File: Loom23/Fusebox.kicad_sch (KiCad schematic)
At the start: 0 parts

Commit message: Added detailed version of schematic
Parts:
- added F? (x8): (no value), symbol Device:Fuse
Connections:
- new net ECU+12V: F?.2
- new net From LVMS: F?.1, F?.1, F?.2
- new net Fuel pump power: F?.2
- new net Fused +12V: F?.1
- new net INJ 1,3 +12V: F?.2
- new net INJ 2,4 +12V: F?.2
- new net Lambda sensor power: F?.2
- new net Relays fuelpump: F?.1, F?.1
- new net Relays injectors: F?.1, F?.1
- new net Relays power +12V: F?.2
- new net Relays spark: F?.1
- new net Spark+: F?.2

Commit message: Signed-off-by: fst29 <fst29@cam.ac.uk>
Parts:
- F?: value (none) -> 5A (Lambda sensor)
- F?: value (none) -> 5A (INJ 2,4)
- F?: value (none) -> 2A (ECU)
- F?: value (none) -> 5A (INJ 1,3)
- F?: value (none) -> TBD A (Spark)
- F?: value (none) -> 30A (Our circuits)
- F?: value (none) -> 10A (Fuel pump)
- F?: value (none) -> 20A (FP+INJ)
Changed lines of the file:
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@@
       (effects (font (size 1.27 1.27)) (justify left))
     )
-    (property "Value" "" (id 1) (at 189.23 78.7399 0)
+    (property "Value" "5A (Lambda sensor)" (id 1) (at 189.23 78.7399 0)
       (effects (font (size 1.27 1.27)) (justify left))
     )
@@
       (effects (font (size 1.27 1.27)) (justify left))
     )
-    (property "Value" "" (id 1) (at 151.13 78.7399 0)
+    (property "Value" "5A (INJ 2,4)" (id 1) (at 151.13 78.7399 0)
       (effects (font (size 1.27 1.27)) (justify left))
     )
@@
       (effects (font (size 1.27 1.27)) (justify left))
     )
-    (property "Value" "" (id 1) (at 82.55 78.7399 0)
+    (property "Value" "2A (ECU)" (id 1) (at 82.55 78.7399 0)
       (effects (font (size 1.27 1.27)) (justify left))
     )
@@
       (effects (font (size 1.27 1.27)) (justify left))
     )
-    (property "Value" "" (id 1) (at 134.62 78.7399 0)
+    (property "Value" "5A (INJ 1,3)" (id 1) (at 134.62 78.7399 0)
       (effects (font (size 1.27 1.27)) (justify left))
     )
@@
       (effects (font (size 1.27 1.27)) (justify left))
     )
-    (property "Value" "" (id 1) (at 215.9 78.7399 0)
+    (property "Value" "TBD A (Spark)" (id 1) (at 215.9 78.7399 0)
       (effects (font (size 1.27 1.27)) (justify left))
     )
@@
       (effects (font (size 1.27 1.27)) (justify right))
     )
-    (property "Value" "" (id 1) (at 113.03 78.7399 0)
+    (property "Value" "30A (Our circuits)" (id 1) (at 113.03 78.7399 0)
       (effects (font (size 1.27 1.27)) (justify right))
     )
@@
       (effects (font (size 1.27 1.27)) (justify left))
     )
-    (property "Value" "" (id 1) (at 167.64 78.7399 0)
+    (property "Value" "10A (Fuel pump)" (id 1) (at 167.64 78.7399 0)
       (effects (font (size 1.27 1.27)) (justify left))
     )
@@
       (effects (font (size 1.27 1.27)) (justify left))
     )
-    (property "Value" "" (id 1) (at 95.25 78.7399 0)
+    (property "Value" "20A (FP+INJ)" (id 1) (at 95.25 78.7399 0)
       (effects (font (size 1.27 1.27)) (justify left))
     )

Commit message: Added current ratings
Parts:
- F?: value 20A (FP+INJ) -> 50A
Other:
- note added: "(FP+INJ+SPK+LAMBDA+FANS)"
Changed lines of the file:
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@@
     (stroke (width 0) (type default) (color 0 0 0 0))
+  )
+  (text "(FP+INJ+SPK+LAMBDA+FANS)" (at 95.25 81.28 0)
+    (effects (font (size 0.5 0.5)) (justify left bottom))
   )
   (hierarchical_label "Relays injectors" (shape input) (at 132.08 67.31 90)
@@
       (effects (font (size 1.27 1.27)) (justify left))
     )
-    (property "Value" "20A (FP+INJ)" (id 1) (at 95.25 78.7399 0)
+    (property "Value" "50A" (id 1) (at 95.25 78.7399 0)
       (effects (font (size 1.27 1.27)) (justify left))
     )

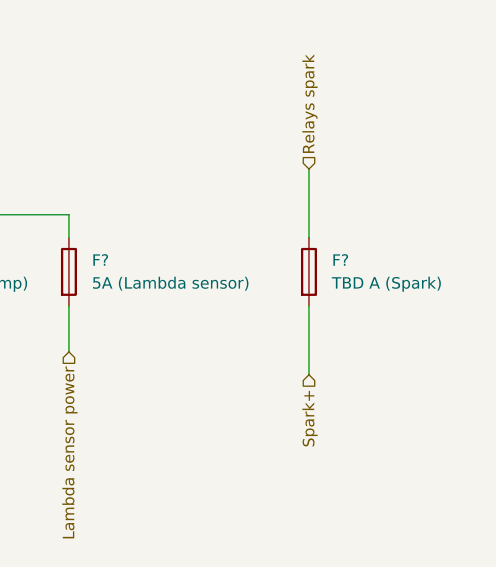
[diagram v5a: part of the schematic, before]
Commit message: Added temp reqs and fuse values
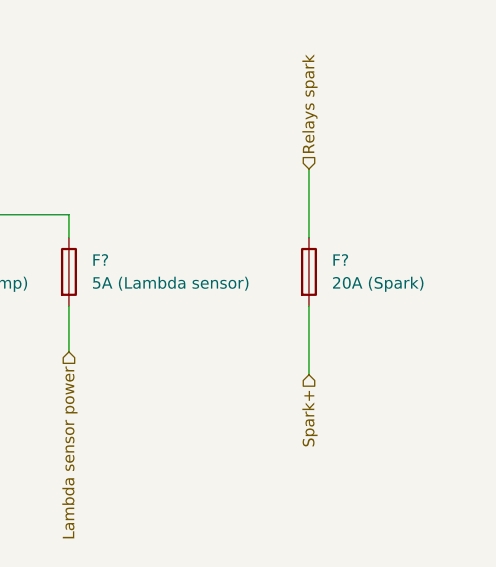
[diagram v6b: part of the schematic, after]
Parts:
- F?: value TBD A (Spark) -> 20A (Spark)
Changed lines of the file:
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@@
       (effects (font (size 1.27 1.27)) (justify left))
     )
-    (property "Value" "TBD A (Spark)" (id 1) (at 215.9 78.7399 0)
+    (property "Value" "20A (Spark)" (id 1) (at 215.9 78.7399 0)
       (effects (font (size 1.27 1.27)) (justify left))
     )

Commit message: Changes made to fusebox, relayboard and camsensor
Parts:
- removed F?: 50A, symbol Device:Fuse
- added F?: 20A (Fans), symbol Device:Fuse
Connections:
- new net Fans: F?.2
- new net Relays fans: F?.1
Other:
- note removed: "(FP+INJ+SPK+LAMBDA+FANS)"
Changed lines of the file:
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@@
 (kicad_sch (version 20211123) (generator eeschema)
   (paper "A4")
-  (junction (at 92.71 68.58) (diameter 0) (color 0 0 0 0)
-  )
   (junction (at 132.08 71.12) (diameter 0) (color 0 0 0 0)
   )
@@
     (stroke (width 0) (type default) (color 0 0 0 0))
   )
+  (wire (pts (xy 233.68 81.28) (xy 233.68 88.9))
+    (stroke (width 0) (type default) (color 0 0 0 0))
+  )
   (wire (pts (xy 213.36 66.04) (xy 213.36 73.66))
     (stroke (width 0) (type default) (color 0 0 0 0))
@@
     (stroke (width 0) (type default) (color 0 0 0 0))
   )
-  (wire (pts (xy 92.71 68.58) (xy 92.71 73.66))
-    (stroke (width 0) (type default) (color 0 0 0 0))
-  )
-  (wire (pts (xy 110.49 68.58) (xy 92.71 68.58))
-    (stroke (width 0) (type default) (color 0 0 0 0))
-  )
   (wire (pts (xy 186.69 81.28) (xy 186.69 86.36))
     (stroke (width 0) (type default) (color 0 0 0 0))
@@
     (stroke (width 0) (type default) (color 0 0 0 0))
   )
-  (wire (pts (xy 92.71 68.58) (xy 80.01 68.58))
+  (wire (pts (xy 80.01 68.58) (xy 110.49 68.58))
     (stroke (width 0) (type default) (color 0 0 0 0))
   )
@@
     (stroke (width 0) (type default) (color 0 0 0 0))
   )
-  (wire (pts (xy 92.71 81.28) (xy 92.71 86.36))
-    (stroke (width 0) (type default) (color 0 0 0 0))
-  )
   (wire (pts (xy 165.1 71.12) (xy 165.1 73.66))
     (stroke (width 0) (type default) (color 0 0 0 0))
   )
+  (wire (pts (xy 233.68 66.04) (xy 233.68 73.66))
+    (stroke (width 0) (type default) (color 0 0 0 0))
+  )
   (wire (pts (xy 148.59 81.28) (xy 148.59 86.36))
     (stroke (width 0) (type default) (color 0 0 0 0))
@@
     (stroke (width 0) (type default) (color 0 0 0 0))
   )
-  (text "(FP+INJ+SPK+LAMBDA+FANS)" (at 95.25 81.28 0)
-    (effects (font (size 0.5 0.5)) (justify left bottom))
-  )
   (hierarchical_label "Relays injectors" (shape input) (at 132.08 67.31 90)
     (effects (font (size 1.27 1.27)) (justify left))
   )
+  (hierarchical_label "Relays fans" (shape input) (at 233.68 66.04 90)
+    (effects (font (size 1.27 1.27)) (justify left))
+  )
   (hierarchical_label "INJ 2,4 +12V" (shape input) (at 148.59 86.36 270)
     (effects (font (size 1.27 1.27)) (justify right))
   )
+  (hierarchical_label "Fans" (shape input) (at 233.68 88.9 270)
+    (effects (font (size 1.27 1.27)) (justify right))
+  )
   (hierarchical_label "Fuel pump power" (shape input) (at 165.1 86.36 270)
     (effects (font (size 1.27 1.27)) (justify right))
@@
     (effects (font (size 1.27 1.27)) (justify right))
   )
-  (hierarchical_label "Relays power +12V" (shape input) (at 92.71 86.36 270)
-    (effects (font (size 1.27 1.27)) (justify right))
-  )
   (hierarchical_label "Fused +12V" (shape input) (at 110.49 86.36 270)
     (effects (font (size 1.27 1.27)) (justify right))
@@
     )
     (property "Datasheet" "~" (id 3) (at 186.69 77.47 0)
+      (effects (font (size 1.27 1.27)) hide)
+    )
+    (pin "1")
+    (pin "2")
+  )
+  (symbol (lib_id "Device:Fuse") (at 233.68 77.47 0) (unit 1)
+    (in_bom yes) (on_board yes) (fields_autoplaced)
+    (property "Reference" "F?" (id 0) (at 236.22 76.1999 0)
+      (effects (font (size 1.27 1.27)) (justify left))
+    )
+    (property "Value" "20A (Fans)" (id 1) (at 236.22 78.7399 0)
+      (effects (font (size 1.27 1.27)) (justify left))
+    )
+    (property "Footprint" "" (id 2) (at 231.902 77.47 90)
+      (effects (font (size 1.27 1.27)) hide)
+    )
+    (property "Datasheet" "~" (id 3) (at 233.68 77.47 0)
       (effects (font (size 1.27 1.27)) hide)
     )
@@
       (effects (font (size 1.27 1.27)) hide)
     )
-    (pin "1")
-    (pin "2")
-  )
-  (symbol (lib_id "Device:Fuse") (at 92.71 77.47 0) (unit 1)
-    (in_bom yes) (on_board yes) (fields_autoplaced)
-    (property "Reference" "F?" (id 0) (at 95.25 76.1999 0)
-      (effects (font (size 1.27 1.27)) (justify left))
-    )
-    (property "Value" "50A" (id 1) (at 95.25 78.7399 0)
-      (effects (font (size 1.27 1.27)) (justify left))
-    )
-    (property "Footprint" "" (id 2) (at 90.932 77.47 90)
-      (effects (font (size 1.27 1.27)) hide)
-    )
-    (property "Datasheet" "~" (id 3) (at 92.71 77.47 0)
-      (effects (font (size 1.27 1.27)) hide)
-    )

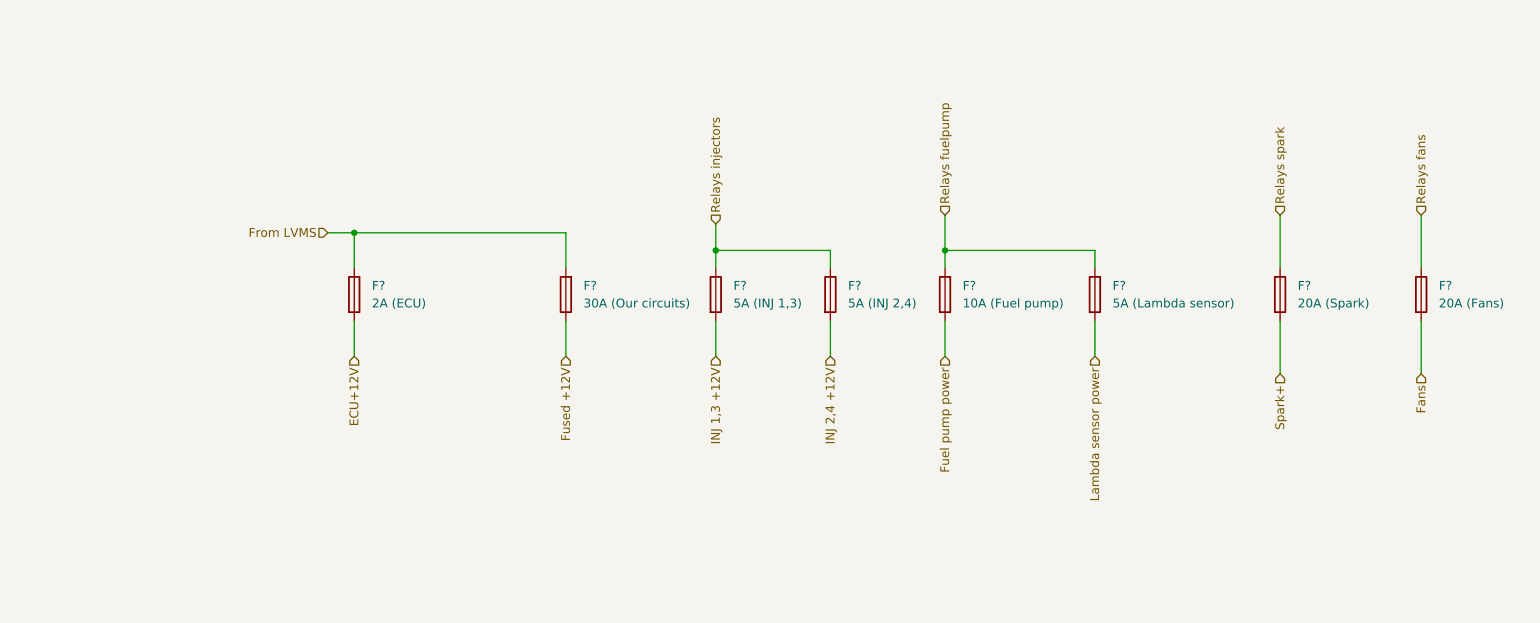
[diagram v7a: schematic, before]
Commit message: Changed labels to match old wires
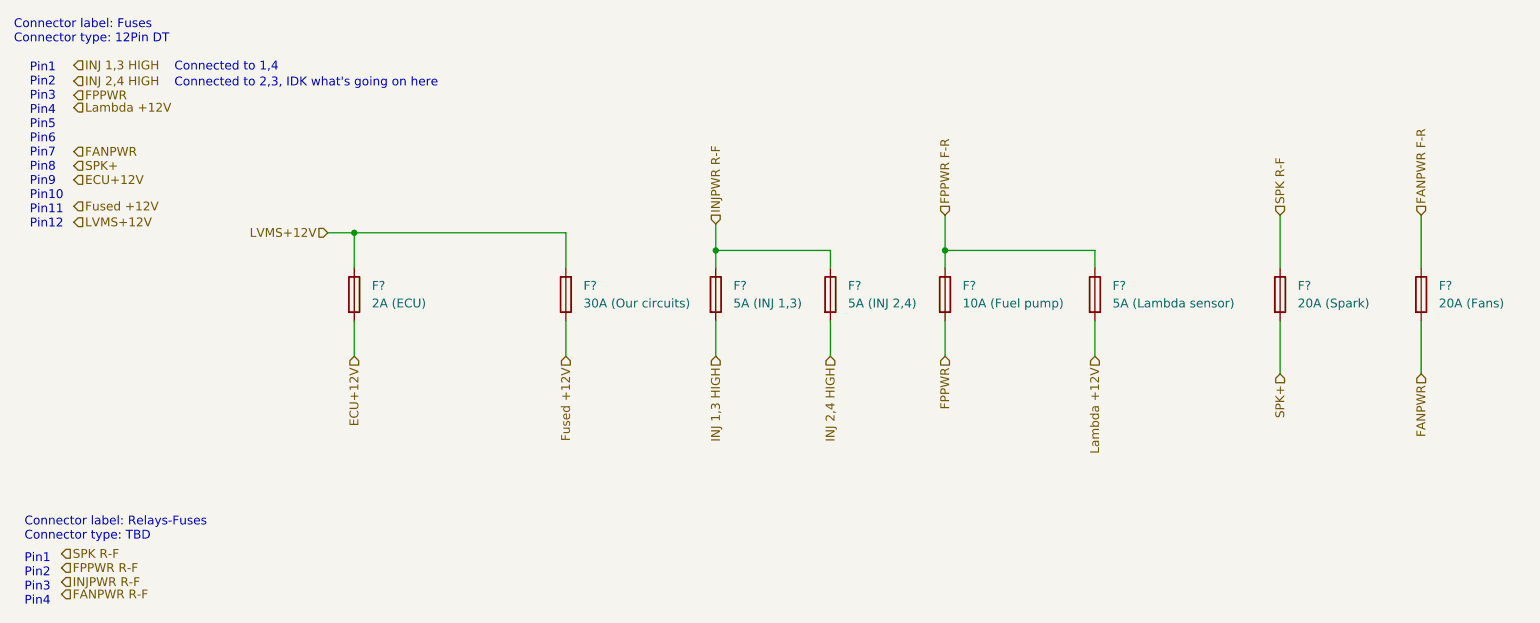
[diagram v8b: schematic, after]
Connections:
- net Fans renamed FANPWR
- net From LVMS renamed LVMS+12V
- net Fuel pump power renamed FPPWR
- net INJ 1,3 +12V renamed INJ 1,3 HIGH
- net INJ 2,4 +12V renamed INJ 2,4 HIGH
- net Lambda sensor power renamed Lambda +12V
- net Relays fans renamed FANPWR F-R
- net Relays fuelpump renamed FPPWR F-R
- net Relays injectors renamed INJPWR R-F
- net Relays spark renamed SPK R-F
- net Spark+ renamed SPK+
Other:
- note added: "Connected to 1,4"
- note added: "Connected to 2,3, IDK what's going on here"
- note added: "Connector label: Fuses Connector type: 12Pin DT"
- note added: "Connector label: Relays-Fuses Connector type: TBD"
- note added: "Pin1 Pin2 Pin3 Pin4"
- note added: "Pin1 Pin2 Pin3 Pin4 Pin5 Pin6 Pin7 Pin8 Pin9 Pin10 Pin11 Pin12"
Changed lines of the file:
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@@
     (stroke (width 0) (type default) (color 0 0 0 0))
   )
-  (hierarchical_label "Relays injectors" (shape input) (at 132.08 67.31 90)
+  (text "Connected to 1,4\n" (at 54.102 45.466 0)
+    (effects (font (size 1.27 1.27)) (justify left bottom))
+  )
+  (text "Pin1\nPin2\nPin3\nPin4\nPin5\nPin6\nPin7\nPin8\nPin9\nPin10\nPin11\nPin12"
+    (at 33.274 68.072 0)
+    (effects (font (size 1.27 1.27)) (justify left bottom))
+  )
+  (text "Pin1\nPin2\nPin3\nPin4\n\n\n" (at 32.512 126.492 0)
+    (effects (font (size 1.27 1.27)) (justify left bottom))
+  )
+  (text "Connector label: Fuses\nConnector type: 12Pin DT\n" (at 30.988 41.402 0)
+    (effects (font (size 1.27 1.27)) (justify left bottom))
+  )
+  (text "Connector label: Relays-Fuses\nConnector type: TBD\n"
+    (at 32.512 113.03 0)
+    (effects (font (size 1.27 1.27)) (justify left bottom))
+  )
+  (text "Connected to 2,3, IDK what's going on here\n" (at 54.102 47.752 0)
+    (effects (font (size 1.27 1.27)) (justify left bottom))
+  )
+  (hierarchical_label "INJPWR R-F" (shape input) (at 132.08 67.31 90)
     (effects (font (size 1.27 1.27)) (justify left))
   )
-  (hierarchical_label "Relays fans" (shape input) (at 233.68 66.04 90)
+  (hierarchical_label "ECU+12V" (shape input) (at 39.624 60.96 0)
     (effects (font (size 1.27 1.27)) (justify left))
   )
-  (hierarchical_label "INJ 2,4 +12V" (shape input) (at 148.59 86.36 270)
+  (hierarchical_label "FANPWR" (shape input) (at 39.624 56.896 0)
+    (effects (font (size 1.27 1.27)) (justify left))
+  )
+  (hierarchical_label "FANPWR F-R" (shape input) (at 233.68 66.04 90)
+    (effects (font (size 1.27 1.27)) (justify left))
+  )
+  (hierarchical_label "INJ 2,4 HIGH" (shape input) (at 39.624 46.736 0)
+    (effects (font (size 1.27 1.27)) (justify left))
+  )
+  (hierarchical_label "INJ 2,4 HIGH" (shape input) (at 148.59 86.36 270)
     (effects (font (size 1.27 1.27)) (justify right))
   )
-  (hierarchical_label "Fans" (shape input) (at 233.68 88.9 270)
+  (hierarchical_label "FANPWR" (shape input) (at 233.68 88.9 270)
     (effects (font (size 1.27 1.27)) (justify right))
   )
-  (hierarchical_label "Fuel pump power" (shape input) (at 165.1 86.36 270)
+  (hierarchical_label "FPPWR" (shape input) (at 165.1 86.36 270)
     (effects (font (size 1.27 1.27)) (justify right))
   )
-  (hierarchical_label "From LVMS" (shape input) (at 76.2 68.58 180)
+  (hierarchical_label "LVMS+12V" (shape input) (at 76.2 68.58 180)
     (effects (font (size 1.27 1.27)) (justify right))
   )
-  (hierarchical_label "Lambda sensor power" (shape input) (at 186.69 86.36 270)
+  (hierarchical_label "SPK R-F" (shape input) (at 37.846 114.808 0)
+    (effects (font (size 1.27 1.27)) (justify left))
+  )
+  (hierarchical_label "LVMS+12V" (shape input) (at 39.624 67.056 0)
+    (effects (font (size 1.27 1.27)) (justify left))
+  )
+  (hierarchical_label "Lambda +12V" (shape input) (at 186.69 86.36 270)
     (effects (font (size 1.27 1.27)) (justify right))
+  )
+  (hierarchical_label "SPK+" (shape input) (at 39.624 58.928 0)
+    (effects (font (size 1.27 1.27)) (justify left))
+  )
+  (hierarchical_label "INJPWR R-F" (shape input) (at 37.846 118.872 0)
+    (effects (font (size 1.27 1.27)) (justify left))
   )
   (hierarchical_label "Fused +12V" (shape input) (at 110.49 86.36 270)
     (effects (font (size 1.27 1.27)) (justify right))
   )
-  (hierarchical_label "Relays spark" (shape input) (at 213.36 66.04 90)
+  (hierarchical_label "INJ 1,3 HIGH" (shape input) (at 39.624 44.45 0)
     (effects (font (size 1.27 1.27)) (justify left))
   )
-  (hierarchical_label "Spark+" (shape input) (at 213.36 88.9 270)
+  (hierarchical_label "SPK R-F" (shape input) (at 213.36 66.04 90)
+    (effects (font (size 1.27 1.27)) (justify left))
+  )
+  (hierarchical_label "SPK+" (shape input) (at 213.36 88.9 270)
     (effects (font (size 1.27 1.27)) (justify right))
   )
-  (hierarchical_label "INJ 1,3 +12V" (shape input) (at 132.08 86.36 270)
+  (hierarchical_label "INJ 1,3 HIGH" (shape input) (at 132.08 86.36 270)
     (effects (font (size 1.27 1.27)) (justify right))
+  )
+  (hierarchical_label "FPPWR R-F" (shape input) (at 37.846 116.84 0)
+    (effects (font (size 1.27 1.27)) (justify left))
   )
   (hierarchical_label "ECU+12V" (shape input) (at 80.01 86.36 270)
     (effects (font (size 1.27 1.27)) (justify right))
   )
-  (hierarchical_label "Relays fuelpump" (shape input) (at 165.1 66.04 90)
+  (hierarchical_label "Fused +12V" (shape input) (at 39.624 64.77 0)
     (effects (font (size 1.27 1.27)) (justify left))
   )
+  (hierarchical_label "FANPWR R-F" (shape input) (at 37.846 120.65 0)
+    (effects (font (size 1.27 1.27)) (justify left))
+  )
+  (hierarchical_label "FPPWR" (shape input) (at 39.624 48.768 0)
+    (effects (font (size 1.27 1.27)) (justify left))
+  )
+  (hierarchical_label "FPPWR F-R" (shape input) (at 165.1 66.04 90)
+    (effects (font (size 1.27 1.27)) (justify left))
+  )
+  (hierarchical_label "Lambda +12V" (shape input) (at 39.624 50.546 0)
+    (effects (font (size 1.27 1.27)) (justify left))
+  )
